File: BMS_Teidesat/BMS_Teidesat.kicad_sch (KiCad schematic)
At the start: 29 parts, among them IC1 ADA4570BRZ-R7, IC2 CSD86311W1723, IC3 ADA4940-1ACPZ-R7, IC4 ADA4940-1ACPZ-R7, IC5 AD8605ACBZ-REEL7, IC7 AD7091R-8BCPZ-RL7, J1 Battery, U1 DS18B20

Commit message: Esquemático 2
Se finalizó la rama del amplificador R-R añadiendo al ganancia final y se comenzó con la rama de la sonda Hall

Co-Authored-By: hugohdezmo <238262256+hugohdezmo@users.noreply.github.com>
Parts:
- removed IC1: ADA4570BRZ-R7, Huellas BMS:SOIC127P600X175-8N, symbol ADA4570BRZ-R7:ADA4570BRZ-R7
- removed IC4: ADA4940-1ACPZ-R7, Huellas BMS:QFN50P300X300X80-17N-D, symbol ADA4940-1ACPZ-R7:ADA4940-1ACPZ-R7
- added C3: 10n, symbol Device:C
- added IC1: AD8606ARMZ-REEL, SOP65P490X110-8N, symbol AD8606ARMZ-REEL:AD8606ARMZ-REEL
- added IC6: ACS758LCB-100U-PFF-T, symbol ACS758LCB-100U-PFF-T:ACS758LCB-100U-PFF-T
- added R10, R13: 210, symbol Device:R
- added R11, R14: 1000, symbol Device:R
- added R12, R9: 1870, symbol Device:R
- added R15: 100, symbol Device:R
- added R16, R18: 80,6K, symbol Device:R
- added R17: 50,5k, symbol Device:R
- added R19: 50,5K, symbol Device:R
- R5: value R -> 40,2K
- R6: value R -> 10K
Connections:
- net +3V3: now also IC7.1 (VDD), IC6.1 (VCC); no longer R5.2
- net +5V: now also IC1.8 (V+)
- net +Battery: now also R10.1; no longer IC3.4 (+FB)
- net +Sonda: now also IC1.7 (OUT_B), R19.2
- net -Battery: now also R13.1; no longer IC3.1 (-FB)
- net GND: now also R6.2, C3.1, IC1.4 (V-), IC6.2 (GND), R17.1; no longer R6.1
- net at IC3.2 (+IN), IC5.1 (OUT): now also R11.2
- net REFOUT: now reaches IC7.3 (REFIN/REFOUT)
- net REFOUT: now also R5.1
- net at IC3.3 (-IN): now also R14.2
- removed net VOCM2: R5.1, R6.2
- new net: IC1.6 (-IN_B), R18.2, R19.1
- new net: IC6.3 (VIOUT), R15.1
- new net: C3.2, R15.2, R16.1
- new net: IC1.1 (OUT_A), IC1.2 (-IN_A), R18.1
- new net: R12.1, R13.2
- new net: R10.2, R9.1
- new net: IC3.4 (+FB), R11.1, R9.2
- new net: IC1.3 (+IN_A), R5.2, R6.1
- new net: IC1.5 (+IN_B), R16.2, R17.2
- new net: IC3.1 (-FB), R12.2, R14.1
- no-connect marks 16 -> 12
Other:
- note added: "0.5V estables"
- note added: "0.5V inestables"
- note added: "2.5V siempre"
- note added: "Ganancia 2.08"
- note added: "Restador y atenuador"
- note removed: "Sonda Hall"
- moved on the sheet: C2, IC3, IC5, IC7, J1, R2, R3, R4, R7, R8

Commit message: Esquemático 3
Implementados los arreglos propuestos por Salvador y añadido el microcontrolador

Co-Authored-By: hugohdezmo <238262256+hugohdezmo@users.noreply.github.com>
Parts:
- removed D1: RURG5060-F085, Huellas BMS:RURG5060F085, symbol RURG5060-F085:RURG5060-F085
- removed IC1: AD8606ARMZ-REEL, SOP65P490X110-8N, symbol AD8606ARMZ-REEL:AD8606ARMZ-REEL
- removed IC6: ACS758LCB-100U-PFF-T, symbol ACS758LCB-100U-PFF-T:ACS758LCB-100U-PFF-T
- removed U1: DS18B20, Package_TO_SOT_THT:TO-92_Inline, symbol Sensor_Temperature:DS18B20
- added C4: 10n, Capacitor_SMD:CP_Elec_3x5.3, symbol Device:C
- added C9: 10u, symbol Device:C
- added D1, D2: SS14, Huellas BMS:DIOM8059X256N, symbol Diode:SS14
- added J2: Battery, Connector_PinSocket_1.00mm:PinSocket_1x02_P1.00mm_Vertical_SMD_Pin1Left, symbol Connector:Conn_01x02_Pin
- added R21: 10, Resistor_SMD:R_0201_0603Metric, symbol Device:R
- added R5: 10k, Resistor_SMD:R_0201_0603Metric, symbol Device:R
- added Termistor1: 10k, Resistor_SMD:R_0201_0603Metric, symbol Device:Thermistor_NTC
- added U2: AD8606ARMZ-REEL, Huellas BMS:SOP65P490X110-8N, symbol AD8606ARMZ-REEL:AD8606ARMZ-REEL
- added U4: ACS37002LMCATR-050B5, Huellas BMS:ACS37002LMCA050U5, symbol ACS37002LMCATR-050B5:ACS37002LMCATR-050B5
- added U7: AD8605ACBZ-REEL7, Huellas BMS:AD8605ACBZREEL7, symbol AD8605ACBZ-REEL7:AD8605ACBZ-REEL7
- added U8: TMS5703137DZWTQQ1, Huellas BMS:BGA337C80P19X19_1600X1600X140, symbol TMS5703137DZWTQQ1:TMS5703137DZWTQQ1
- C1: renamed from C2; value C -> 1n; footprint (none) -> Capacitor_SMD:CP_Elec_3x5.3
- C2: renamed from C3; value 10n -> 1n; footprint (none) -> Capacitor_SMD:CP_Elec_3x5.3
- C3: renamed from C1; value C -> 10n; footprint (none) -> Capacitor_SMD:CP_Elec_3x5.3
- J1: footprint (none) -> Connector_PinSocket_1.00mm:PinSocket_1x02_P1.00mm_Vertical_SMD_Pin1Left
- R1: renamed from R2; value R -> 100; footprint (none) -> Resistor_SMD:R_0201_0603Metric
- R10: renamed from R5; footprint (none) -> Resistor_SMD:R_0201_0603Metric
- R11: renamed from R6; footprint (none) -> Resistor_SMD:R_0201_0603Metric
- R12: renamed from R14; footprint (none) -> Resistor_SMD:R_0201_0603Metric
- R13: renamed from R15; footprint (none) -> Resistor_SMD:R_0201_0603Metric
- R14: renamed from R13; footprint (none) -> Resistor_SMD:R_0201_0603Metric
- R15: renamed from R12; footprint (none) -> Resistor_SMD:R_0201_0603Metric
- R16: renamed from R9; footprint (none) -> Resistor_SMD:R_0201_0603Metric
- R17: renamed from R10; footprint (none) -> Resistor_SMD:R_0201_0603Metric
- R18: renamed from R4; value R -> 10K; footprint (none) -> Resistor_SMD:R_0201_0603Metric
- R19: renamed from R3; value R -> 10K; footprint (none) -> Resistor_SMD:R_0201_0603Metric
- R2: renamed from R19; footprint (none) -> Resistor_SMD:R_0201_0603Metric
- R20: renamed from R1; value R -> 10; footprint (none) -> Resistor_SMD:R_0201_0603Metric
- R3: renamed from R17; footprint (none) -> Resistor_SMD:R_0201_0603Metric
- R4: renamed from R18; footprint (none) -> Resistor_SMD:R_0201_0603Metric
- R6: renamed from R7; value R -> 10K; footprint (none) -> Resistor_SMD:R_0201_0603Metric
- R7: renamed from R8; value R -> 10K; footprint (none) -> Resistor_SMD:R_0201_0603Metric
- R8: renamed from R16; footprint (none) -> Resistor_SMD:R_0201_0603Metric
- R9: renamed from R11; footprint (none) -> Resistor_SMD:R_0201_0603Metric
- renumbered C8 to C5, C9 to C6, C10 to C7, C11 to C8, IC5 to U1, IC3 to U3, IC7 to U5, IC2 to U6
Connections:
- net +3V3: now also U7.5 (V+); no longer R18.2, U3.5 (+VS_1), U3.6 (+VS_2), U3.7 (+VS_3), U3.8 (+VS_4)
- net +5V: now also R18.2, U3.5 (+VS_1), U3.6 (+VS_2), U3.7 (+VS_3), U3.8 (+VS_4), U2.8 (V+), U4.10 (VCC)
- net +Battery: now also J2.1 (Pin_1), U4.1 (IP+_1), U4.2 (IP+_2), U4.3 (IP+_3), U4.4 (IP+_4); no longer R17.1, U3.10 (+OUT), U5.15 (VIN1)
- net +Sonda: now also U2.3 (+IN_A)
- net GND: now also U5.17 (GND_2), U5.25 (EP), U5.4 (GND_1), C9.2, Termistor1.2, U2.4 (V-), U4.15 (GND), U7.2 (V-)
- net REFOUT: now also R5.2
- net at R2.1, R4.2: now also U2.2 (-IN_A)
- net at R13.1: now also U4.12 (VIOUT)
- net at R4.1: now also U2.5 (+IN_B)
- net Control: now reaches U6.A1 (GATE_1)
- net Control: now also U6.C1 (GATE_2)
- net at U6.A2 (DRAIN_1_1): now also C3.1, D1.2 (A), J2.2 (Pin_2)
- net at U6.B1 (SOURCE_1): now also R20.2, U6.C2 (DRAIN_2_1), D1.1 (K), D2.1 (K), R21.2
- net LOAD-: now reaches U6.B2 (SOURCE_2)
- net LOAD-: now also C4.1, D2.2 (A)
- net at C3.2: now also R20.1
- net at R10.2, R11.1: now also U2.7 (OUT_B)
- net at R3.2, R8.2: now also U2.1 (OUT_A)
- net Mosi MC: now reaches U5.18 (SDI)
- net Salida CAD: now reaches U5.19 (SDO)
- net at U5.2 (REGCAP): now also C9.1
- net Reloj MC: now reaches U5.20 (SCLK)
- net GIO1 MC: now reaches U5.21 (~{CONVST})
- net GIO2 MC: now reaches U5.22 (VDRIVE)
- net GIO3 MC: now reaches U5.23 (~{CS})
- net GIO4 MC: now reaches U5.24 (~{RESET})
- net +VBat: now reaches U5.6 (VIN0)
- net +VBat: now also R17.1, U3.10 (+OUT)
- net -Battery renamed -VBat
- new net: R5.1, Termistor1.1, U7.3 (+IN)
- new net: C4.2, R21.1
- new net +LOAD: U4.5 (IP-_1), U4.6 (IP-_2), U4.7 (IP-_3), U4.8 (IP-_4)
- new net Temp: U5.15 (VIN1), U7.1 (OUT), U7.4 (-IN)
- no-connect marks 12 -> 28
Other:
- note added: "CIRCUITO DE POTENCIA"
- note added: "Es importante que fisicamente esten cerca del transistor"
- note added: "Hugo Hernández Morales Ángel Castro Vega TEIDESAT"
- note added: "LECTOR DE CORRIENTE"
- note added: "LECTOR DE TEMPERATURA"
- note added: "LECTOR DE VOLTAJE"
- note added: "Los valores actuales son una recomendación"
- note added: "MICROCONTROLADOR"
- note added: "MOSFETs"
- note added: "Para el calculo de las R y C en la red de Snubber es necesario medir los picos de voltaje de la placa mientras se apagan los mosfet con un osciloscopio y calcular los valores de R y C usando esa medida"
- note added: "Placa BMS del nanosatélite Teidesat"
- note added: "Previsión de conexiones"
- note removed: "MOSFET"
- note removed: "No se ha encontrado símbolo ni huella del sensor de temperatura escogido"
- moved on the sheet: C2, C3, R10, R11, R13, R2, R20, R3, R4, R8, U5, U6

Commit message: Modificación de etiquetas y nuevo micro
Se han puesto correctamente las etiquetas, todas en ingles en mayúsculas y con el cable debajo. Además de poner el correcto símbolo y huella del micro
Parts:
- removed U8: TMS5703137DZWTQQ1, Huellas BMS:BGA337C80P19X19_1600X1600X140, symbol TMS5703137DZWTQQ1:TMS5703137DZWTQQ1
- added IC1: TMS5703137DPGEQQ1, Huellas BMS:QFP50P2200X2200X160-144N, symbol TMS5703137DPGEQQ1:TMS5703137DPGEQQ1
- C9: footprint (none) -> Capacitor_SMD:C_0805_2012Metric
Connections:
- net +Battery renamed +BATTERY
- net +Sonda renamed +HALL
- net +VBat renamed +VBAT
- net -VBat renamed -VBAT
- net Control renamed CONTROL
- net Mosi MC renamed MOSI MC
- net Reloj MC renamed CLOCK MC
- net Salida CAD renamed OUT CAD
- net Temp renamed TEMP

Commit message: Conexiones micro y sensor de corriente implementado
Conectamos el sensor de corriente entre los MOSFETS del circuito de potencia y conectamos el CAD al microcontrolador

Co-Authored-By: hugohdezmo <238262256+hugohdezmo@users.noreply.github.com>
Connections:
- net GIO1 MC is gone; now on net GIOA: U5.21 (~{CONVST})
- net GIO2 MC is gone; now on net +3V3: U5.22 (VDRIVE)
- net GIO3 MC is gone; now on net CS: U5.23 (~{CS})
- net GIO4 MC is gone; now on net RESET: U5.24 (~{RESET})
- net +BATTERY: now also D1.1 (K), D2.1 (K), R20.2, R21.2
- net +HALL: now also U2.7 (OUT_B); no longer U2.3 (+IN_A)
- net +LOAD: now also U6.B1 (SOURCE_1), U6.C2 (DRAIN_2_1)
- net CLOCK MC: now also IC1.95 (MIBSPI1CLK)
- net MOSI MC: now also IC1.93 (MIBSPI1SIMO)
- net OUT CAD: now also IC1.94 (MIBSPI1SOMI)
- net at R2.1, R4.2: now also U2.6 (-IN_B); no longer U2.2 (-IN_A)
- net at R3.2, R8.2: now also U2.5 (+IN_B); no longer U2.1 (OUT_A)
- net at R4.1: now also U2.1 (OUT_A), U2.2 (-IN_A); no longer U2.5 (+IN_B)
- net at R10.2, R11.1: now also U2.3 (+IN_A); no longer U2.7 (OUT_B)
- net CS: now reaches IC1.105 (MIBSPI1NCS[0])
- net RESET: now reaches IC1.14 (GIOA[5])
- net GIOA: now reaches IC1.9 (GIOA[2])
- no-connect marks 28 -> 188
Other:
- note removed: "Hugo Hernández Morales Ángel Castro Vega TEIDESAT"
- note removed: "Placa BMS del nanosatélite Teidesat"
- title: (none) -> Placa BMS del nanosatélite Teidesat

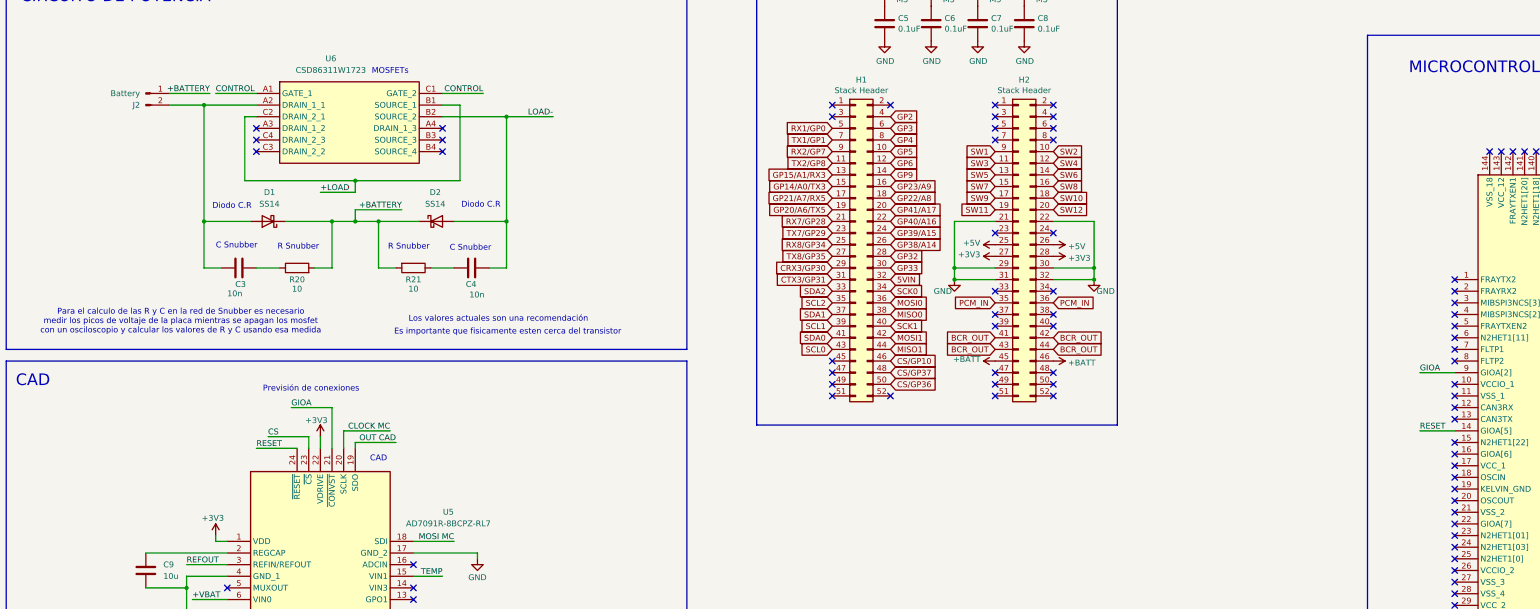
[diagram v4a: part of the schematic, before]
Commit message: Conexión MOSFET al micro
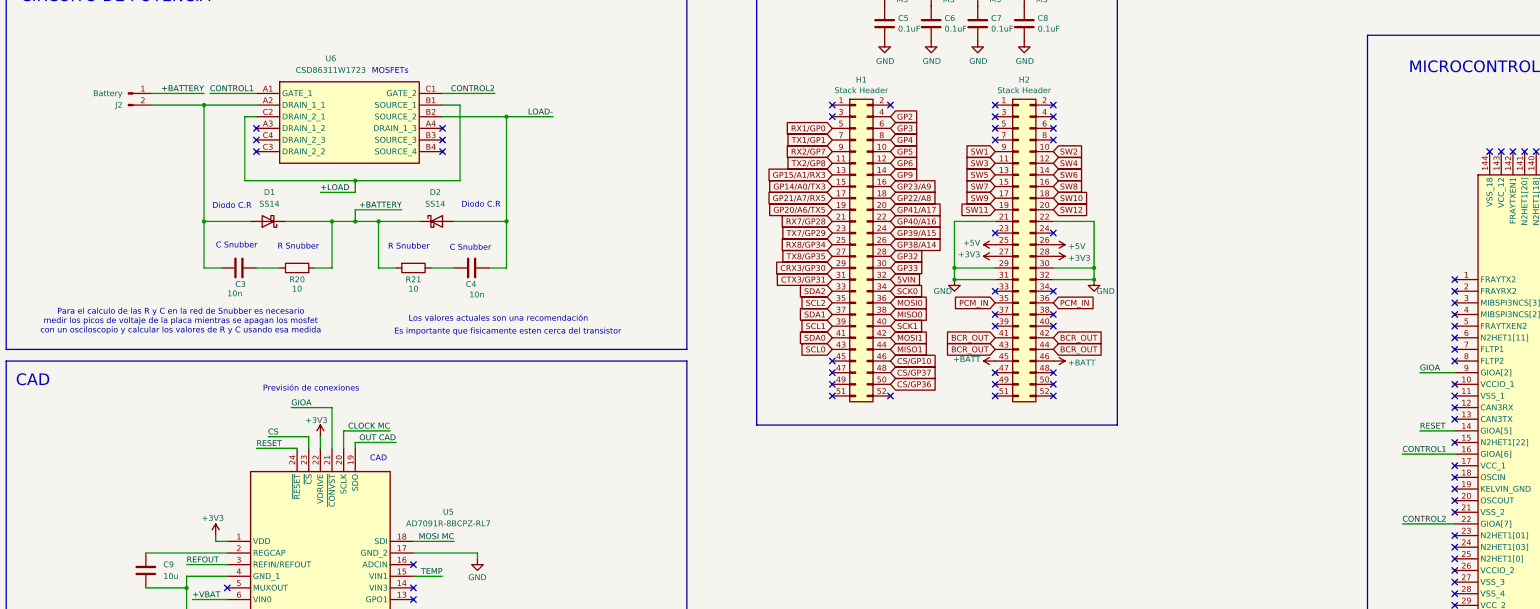
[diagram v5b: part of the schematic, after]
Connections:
- net CONTROL1: now reaches IC1.16 (GIOA[6])
- net CONTROL1: now also U6.A1 (GATE_1)
- net CONTROL2: now reaches IC1.22 (GIOA[7])
- net CONTROL2: now also U6.C1 (GATE_2)
- removed net CONTROL: U6.A1 (GATE_1), U6.C1 (GATE_2)
- no-connect marks 188 -> 186
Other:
- moved on the sheet: J2
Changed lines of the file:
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@@
 	)
 	(no_connect
-		(at 481.33 133.35)
-	)
-	(no_connect
 		(at 539.75 52.07)
 	)
@@
 	)
 	(no_connect
-		(at 481.33 118.11)
-	)
-	(no_connect
 		(at 231.14 180.34)
 	)
@@
 	(wire
 		(pts
-			(xy 200.66 39.37) (xy 209.55 39.37)
+			(xy 469.9 118.11) (xy 481.33 118.11)
+		)
+		(stroke
+			(width 0)
+			(type default)
+		)
+	)
+	(wire
+		(pts
+			(xy 196.85 39.37) (xy 208.28 39.37)
 		)
 		(stroke
@@
 	(wire
 		(pts
-			(xy 210.82 39.37) (xy 219.71 39.37)
+			(xy 209.55 39.37) (xy 219.71 39.37)
 		)
 		(stroke
@@
 	(wire
 		(pts
-			(xy 200.66 41.91) (xy 208.28 41.91)
+			(xy 196.85 41.91) (xy 208.28 41.91)
 		)
 		(stroke
@@
 	(wire
 		(pts
-			(xy 269.24 39.37) (xy 260.35 39.37)
+			(xy 271.78 39.37) (xy 260.35 39.37)
 		)
 		(stroke
@@
 	(wire
 		(pts
+			(xy 469.9 133.35) (xy 481.33 133.35)
+		)
+		(stroke
+			(width 0)
+			(type default)
+		)
+	)
+	(wire
+		(pts
 			(xy 204.47 144.78) (xy 204.47 147.32)
 		)
@@
 	)
 	(label "+BATTERY"
-		(at 209.55 39.37 180)
+		(at 208.28 39.37 180)
 		(effects
 			(font
@@
 		)
 	)
+	(label "CONTROL1"
+		(at 469.9 118.11 0)
+		(effects
+			(font
+				(size 1.27 1.27)
+			)
+			(justify left bottom)
+		)
+	)
 	(label "RESET"
 		(at 473.71 113.03 0)
@@
 		)
 	)
-	(label "CONTROL"
-		(at 269.24 39.37 180)
+	(label "CONTROL2"
+		(at 271.78 39.37 180)
 		(effects
 			(font
@@
 		)
 	)
+	(label "CONTROL2"
+		(at 469.9 133.35 0)
+		(effects
+			(font
+				(size 1.27 1.27)
+			)
+			(justify left bottom)
+		)
+	)
 	(label "CS"
 		(at 222.25 114.3 0)
@@
 		)
 	)
-	(label "CONTROL"
-		(at 210.82 39.37 0)
+	(label "CONTROL1"
+		(at 209.55 39.37 0)
 		(effects
 			(font
@@
 	(symbol
 		(lib_id "Connector:Conn_01x02_Pin")
-		(at 195.58 39.37 0)
+		(at 191.77 39.37 0)
 		(unit 1)
 		(exclude_from_sim no)
@@
 		(fields_autoplaced yes)
 		(property "Reference" "J2"
-			(at 194.31 41.9101 0)
+			(at 190.5 41.9101 0)
 			(effects
 				(font
@@
 		)
 		(property "Value" "Battery"
-			(at 194.31 39.3701 0)
+			(at 190.5 39.3701 0)
 			(effects
 				(font
@@
 		)
 		(property "Footprint" "Connector_PinSocket_1.00mm:PinSocket_1x02_P1.00mm_Vertical_SMD_Pin1Left"
-			(at 195.58 39.37 0)
+			(at 191.77 39.37 0)
 			(effects
 				(font
@@
 		)
 		(property "Datasheet" "~"
-			(at 195.58 39.37 0)
+			(at 191.77 39.37 0)
 			(effects
 				(font
@@
 		)
 		(property "Description" "Generic connector, single row, 01x02, script generated"
-			(at 195.58 39.37 0)
+			(at 191.77 39.37 0)
 			(effects
 				(font

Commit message: Comienzo de enrutado
Co-Authored-By: hugohdezmo <238262256+hugohdezmo@users.noreply.github.com>
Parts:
- added U8: STM32G474VET6, Huellas BMS:QFP50P1600X1600X160-100N, symbol STM32G474VET6:STM32G474VET6
- renumbered IC1 to U9
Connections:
- net +BATTERY: no longer J2.1 (Pin_1)
- net CLOCK MC: no longer U9.95 (MIBSPI1CLK)
- net CONTROL1: no longer U9.16 (GIOA[6])
- net CONTROL2: no longer U9.22 (GIOA[7])
- net CS: no longer U9.105 (MIBSPI1NCS[0])
- net GIOA: no longer U9.9 (GIOA[2])
- net GND: now also J2.2 (Pin_2)
- net MOSI MC: no longer U9.93 (MIBSPI1SIMO)
- net OUT CAD: no longer U9.94 (MIBSPI1SOMI)
- net RESET: no longer U9.14 (GIOA[5])
- net at C3.1, D1.2 (A), U6.A2 (DRAIN_1_1): now also J2.1 (Pin_1); no longer J2.2 (Pin_2)
- net 5VIN: no longer names the net of H1.32 (Pin_32)
- removed net BCR_OUT: H2.41 (Pin_41), H2.42 (Pin_42), H2.43 (Pin_43), H2.44 (Pin_44)
- net CRX3/GP30: no longer names the net of H1.29 (Pin_29)
- net CS/GP10: no longer names the net of H1.46 (Pin_46)
- net CS/GP36: no longer names the net of H1.50 (Pin_50)
- net CS/GP37: no longer names the net of H1.48 (Pin_48)
- net CTX3/GP31: no longer names the net of H1.31 (Pin_31)
- net GP14/A0/TX3: no longer names the net of H1.15 (Pin_15)
- net GP15/A1/RX3: no longer names the net of H1.13 (Pin_13)
- net GP2: no longer names the net of H1.4 (Pin_4)
- net GP20/A6/TX5: no longer names the net of H1.19 (Pin_19)
- net GP21/A7/RX5: no longer names the net of H1.17 (Pin_17)
- net GP22/A8: no longer names the net of H1.18 (Pin_18)
- net GP23/A9: no longer names the net of H1.16 (Pin_16)
- net GP3: no longer names the net of H1.6 (Pin_6)
- net GP32: no longer names the net of H1.28 (Pin_28)
- net GP33: no longer names the net of H1.30 (Pin_30)
- net GP38/A14: no longer names the net of H1.26 (Pin_26)
- net GP39/A15: no longer names the net of H1.24 (Pin_24)
- net GP4: no longer names the net of H1.8 (Pin_8)
- net GP40/A16: no longer names the net of H1.22 (Pin_22)
- net GP41/A17: no longer names the net of H1.20 (Pin_20)
- net GP5: no longer names the net of H1.10 (Pin_10)
- net GP6: no longer names the net of H1.12 (Pin_12)
- net GP9: no longer names the net of H1.14 (Pin_14)
- net LOAD- renamed EPS
- net MISO0: no longer names the net of H1.38 (Pin_38)
- net MISO1: no longer names the net of H1.44 (Pin_44)
- net MOSI0: no longer names the net of H1.36 (Pin_36)
- net MOSI1: no longer names the net of H1.42 (Pin_42)
- net PCM_IN: no longer names the net of H2.35 (Pin_35)
- net PCM_IN: no longer H2.36 (Pin_36)
- net RX1/GP0: no longer names the net of H1.5 (Pin_5)
- net RX2/GP7: no longer names the net of H1.9 (Pin_9)
- net RX7/GP28: no longer names the net of H1.21 (Pin_21)
- net RX8/GP34: no longer names the net of H1.25 (Pin_25)
- net SCK0: no longer names the net of H1.34 (Pin_34)
- net SCK1: no longer names the net of H1.40 (Pin_40)
- net SCL0: no longer names the net of H1.43 (Pin_43)
- net SCL1: no longer names the net of H1.39 (Pin_39)
- net SCL2: no longer names the net of H1.35 (Pin_35)
- net SDA0: no longer names the net of H1.41 (Pin_41)
- net SDA1: no longer names the net of H1.37 (Pin_37)
- net SDA2: no longer names the net of H1.33 (Pin_33)
- net SW1: no longer names the net of H2.9 (Pin_9)
- net SW10: no longer names the net of H2.18 (Pin_18)
- net SW11: no longer names the net of H2.19 (Pin_19)
- net SW12: no longer names the net of H2.20 (Pin_20)
- net SW2: no longer names the net of H2.10 (Pin_10)
- net SW3: no longer names the net of H2.11 (Pin_11)
- net SW4: no longer names the net of H2.12 (Pin_12)
- net SW5: no longer names the net of H2.13 (Pin_13)
- net SW6: no longer names the net of H2.14 (Pin_14)
- net SW7: no longer names the net of H2.15 (Pin_15)
- net SW8: no longer names the net of H2.16 (Pin_16)
- net SW9: no longer names the net of H2.17 (Pin_17)
- net TX1/GP1: no longer names the net of H1.7 (Pin_7)
- net TX2/GP8: no longer names the net of H1.11 (Pin_11)
- net TX7/GP29: no longer names the net of H1.23 (Pin_23)
- net TX8/GP35: no longer names the net of H1.27 (Pin_27)
- no-connect marks 186 -> 356
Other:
- note added: "MICROCONTROLADOR (Teidesat)"
- moved on the sheet: C9, J2, U5

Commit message: Se ha corregido el enrutado de la PCB. Faltan las conexiones de alimentación y de tierra
Co-Authored-By: Angel-Castro-Vega <236372966+Angel-Castro-Vega@users.noreply.github.com>
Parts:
- C1, C2, C3, C4: footprint Capacitor_SMD:CP_Elec_3x5.3 -> Capacitor_SMD:C_0805_2012Metric
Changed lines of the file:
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@@
 			)
 		)
-		(property "Footprint" "Capacitor_SMD:CP_Elec_3x5.3"
+		(property "Footprint" "Capacitor_SMD:C_0805_2012Metric"
 			(at 94.2848 123.19 0)
 			(effects
@@
 			)
 		)
-		(property "Footprint" "Capacitor_SMD:CP_Elec_3x5.3"
+		(property "Footprint" "Capacitor_SMD:C_0805_2012Metric"
 			(at 219.71 76.5048 0)
 			(effects
@@
 			)
 		)
-		(property "Footprint" "Capacitor_SMD:CP_Elec_3x5.3"
+		(property "Footprint" "Capacitor_SMD:C_0805_2012Metric"
 			(at 262.89 78.4352 0)
 			(effects
@@
 			)
 		)
-		(property "Footprint" "Capacitor_SMD:CP_Elec_3x5.3"
+		(property "Footprint" "Capacitor_SMD:C_0805_2012Metric"
 			(at 40.3352 57.15 0)
 			(effects
